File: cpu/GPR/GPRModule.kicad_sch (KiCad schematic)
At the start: 51 parts, among them J1 Interconnect, U1 74HCT574, U10 74HCT245, U11 74HCT125, U2 74HCT574, U3 74HCT245, U4 74HCT245, U5 74HCT245, U6 74HCT245, U7 74HCT245, U8 74HCT245, U9 74HCT245

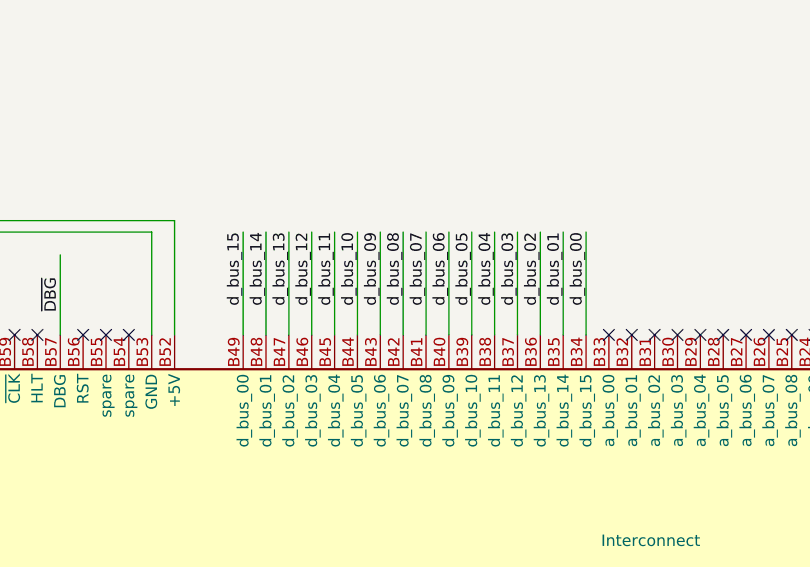
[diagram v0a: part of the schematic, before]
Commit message: GPR v1.4, removed old src, deleted a BOM
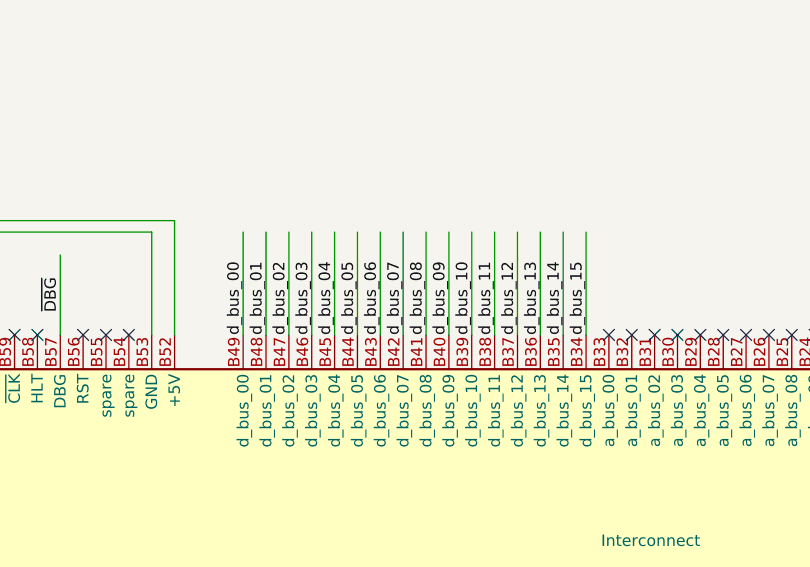
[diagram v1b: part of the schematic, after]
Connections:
- net d_bus_00: now also J1.B49 (d_bus_00); no longer J1.B34 (d_bus_15)
- net d_bus_01: now also J1.B48 (d_bus_01); no longer J1.B35 (d_bus_14)
- net d_bus_02: now also J1.B47 (d_bus_02); no longer J1.B36 (d_bus_13)
- net d_bus_03: now also J1.B46 (d_bus_03); no longer J1.B37 (d_bus_12)
- net d_bus_04: now also J1.B45 (d_bus_04); no longer J1.B38 (d_bus_11)
- net d_bus_05: now also J1.B44 (d_bus_05); no longer J1.B39 (d_bus_10)
- net d_bus_06: now also J1.B43 (d_bus_06); no longer J1.B40 (d_bus_09)
- net d_bus_07: now also J1.B42 (d_bus_07); no longer J1.B41 (d_bus_08)
- net d_bus_08: now also J1.B41 (d_bus_08); no longer J1.B42 (d_bus_07)
- net d_bus_09: now also J1.B40 (d_bus_09); no longer J1.B43 (d_bus_06)
- net d_bus_10: now also J1.B39 (d_bus_10); no longer J1.B44 (d_bus_05)
- net d_bus_11: now also J1.B38 (d_bus_11); no longer J1.B45 (d_bus_04)
- net d_bus_12: now also J1.B37 (d_bus_12); no longer J1.B46 (d_bus_03)
- net d_bus_13: now also J1.B36 (d_bus_13); no longer J1.B47 (d_bus_02)
- net d_bus_14: now also J1.B35 (d_bus_14); no longer J1.B48 (d_bus_01)
- net d_bus_15: now also J1.B34 (d_bus_15); no longer J1.B49 (d_bus_00)
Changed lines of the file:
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@@
     (title "General Purpose Register")
     (date "2020-12-25")
-    (rev "1.3")
+    (rev "1.4")
     (comment 1 "Does not use CLK signal for operation")
   )
@@
     (stroke (width 0) (type default) (color 0 0 0 0))
   )
-  (wire (pts (xy 128.27 194.31) (xy 128.27 182.88))
+  (wire (pts (xy 100.33 182.88) (xy 100.33 194.31))
     (stroke (width 0) (type default) (color 0 0 0 0))
   )
@@
     (stroke (width 0) (type default) (color 0 0 0 0))
   )
-  (wire (pts (xy 115.57 194.31) (xy 115.57 182.88))
+  (wire (pts (xy 113.03 182.88) (xy 113.03 194.31))
     (stroke (width 0) (type default) (color 0 0 0 0))
   )
@@
     (stroke (width 0) (type default) (color 0 0 0 0))
   )
-  (wire (pts (xy 118.11 194.31) (xy 118.11 182.88))
+  (wire (pts (xy 110.49 182.88) (xy 110.49 194.31))
     (stroke (width 0) (type default) (color 0 0 0 0))
   )
@@
     (stroke (width 0) (type default) (color 0 0 0 0))
   )
-  (wire (pts (xy 123.19 194.31) (xy 123.19 182.88))
+  (wire (pts (xy 105.41 182.88) (xy 105.41 194.31))
     (stroke (width 0) (type default) (color 0 0 0 0))
   )
@@
     (stroke (width 0) (type default) (color 0 0 0 0))
   )
-  (wire (pts (xy 120.65 194.31) (xy 120.65 182.88))
+  (wire (pts (xy 107.95 182.88) (xy 107.95 194.31))
     (stroke (width 0) (type default) (color 0 0 0 0))
   )
@@
     (stroke (width 0) (type default) (color 0 0 0 0))
   )
-  (wire (pts (xy 113.03 194.31) (xy 113.03 182.88))
+  (wire (pts (xy 115.57 182.88) (xy 115.57 194.31))
     (stroke (width 0) (type default) (color 0 0 0 0))
   )
@@
     (stroke (width 0) (type default) (color 0 0 0 0))
   )
-  (wire (pts (xy 107.95 194.31) (xy 107.95 182.88))
+  (wire (pts (xy 120.65 182.88) (xy 120.65 194.31))
     (stroke (width 0) (type default) (color 0 0 0 0))
   )
@@
     (stroke (width 0) (type default) (color 0 0 0 0))
   )
-  (wire (pts (xy 102.87 194.31) (xy 102.87 182.88))
+  (wire (pts (xy 125.73 182.88) (xy 125.73 194.31))
     (stroke (width 0) (type default) (color 0 0 0 0))
   )
@@
     (stroke (width 0) (type default) (color 0 0 0 0))
   )
-  (wire (pts (xy 130.81 194.31) (xy 130.81 182.88))
+  (wire (pts (xy 97.79 182.88) (xy 97.79 194.31))
     (stroke (width 0) (type default) (color 0 0 0 0))
   )
@@
     (stroke (width 0) (type default) (color 0 0 0 0))
   )
-  (wire (pts (xy 100.33 194.31) (xy 100.33 182.88))
+  (wire (pts (xy 128.27 182.88) (xy 128.27 194.31))
     (stroke (width 0) (type default) (color 0 0 0 0))
   )
@@
     (stroke (width 0) (type default) (color 0 0 0 0))
   )
-  (wire (pts (xy 110.49 194.31) (xy 110.49 182.88))
+  (wire (pts (xy 118.11 182.88) (xy 118.11 194.31))
     (stroke (width 0) (type default) (color 0 0 0 0))
   )
@@
     (stroke (width 0) (type default) (color 0 0 0 0))
   )
-  (wire (pts (xy 125.73 194.31) (xy 125.73 182.88))
+  (wire (pts (xy 102.87 182.88) (xy 102.87 194.31))
     (stroke (width 0) (type default) (color 0 0 0 0))
   )
@@
     (stroke (width 0) (type default) (color 0 0 0 0))
   )
-  (wire (pts (xy 95.25 194.31) (xy 95.25 182.88))
+  (wire (pts (xy 133.35 182.88) (xy 133.35 194.31))
     (stroke (width 0) (type default) (color 0 0 0 0))
   )
@@
     (stroke (width 0) (type default) (color 0 0 0 0))
   )
-  (wire (pts (xy 105.41 194.31) (xy 105.41 182.88))
+  (wire (pts (xy 123.19 182.88) (xy 123.19 194.31))
     (stroke (width 0) (type default) (color 0 0 0 0))
   )
@@
     (stroke (width 0) (type default) (color 0 0 0 0))
   )
-  (wire (pts (xy 97.79 194.31) (xy 97.79 182.88))
+  (wire (pts (xy 130.81 182.88) (xy 130.81 194.31))
     (stroke (width 0) (type default) (color 0 0 0 0))
   )
@@
     (stroke (width 0) (type default) (color 0 0 0 0))
   )
-  (wire (pts (xy 133.35 194.31) (xy 133.35 182.88))
+  (wire (pts (xy 95.25 182.88) (xy 95.25 194.31))
     (stroke (width 0) (type default) (color 0 0 0 0))
   )
@@
     (effects (font (size 1.27 1.27)) (justify right bottom))
   )
-  (label "d_bus_01" (at 130.81 182.88 270)
-    (effects (font (size 1.27 1.27)) (justify right bottom))
-  )
-  (label "d_bus_11" (at 105.41 182.88 270)
-    (effects (font (size 1.27 1.27)) (justify right bottom))
+  (label "d_bus_01" (at 97.79 194.31 90)
+    (effects (font (size 1.27 1.27)) (justify left bottom))
+  )
+  (label "d_bus_11" (at 123.19 194.31 90)
+    (effects (font (size 1.27 1.27)) (justify left bottom))
   )
   (label "y_bus_12" (at 342.9 30.48 270)
@@
     (effects (font (size 1.27 1.27)) (justify left bottom))
   )
-  (label "d_bus_04" (at 123.19 182.88 270)
-    (effects (font (size 1.27 1.27)) (justify right bottom))
+  (label "d_bus_04" (at 105.41 194.31 90)
+    (effects (font (size 1.27 1.27)) (justify left bottom))
   )
   (label "d_bus_02" (at 49.53 137.16 90)
@@
     (effects (font (size 1.27 1.27)) (justify left bottom))
   )
-  (label "d_bus_00" (at 133.35 182.88 270)
-    (effects (font (size 1.27 1.27)) (justify right bottom))
+  (label "d_bus_00" (at 95.25 194.31 90)
+    (effects (font (size 1.27 1.27)) (justify left bottom))
   )
   (label "x_bus_09" (at 118.11 251.46 90)
@@
     (effects (font (size 1.27 1.27)) (justify right bottom))
   )
-  (label "d_bus_15" (at 95.25 182.88 270)
-    (effects (font (size 1.27 1.27)) (justify right bottom))
+  (label "d_bus_15" (at 133.35 194.31 90)
+    (effects (font (size 1.27 1.27)) (justify left bottom))
   )
   (label "x_bus_04" (at 105.41 251.46 90)
@@
     (effects (font (size 1.27 1.27)) (justify right bottom))
   )
-  (label "d_bus_12" (at 102.87 182.88 270)
-    (effects (font (size 1.27 1.27)) (justify right bottom))
+  (label "d_bus_12" (at 125.73 194.31 90)
+    (effects (font (size 1.27 1.27)) (justify left bottom))
   )
   (label "d_bus_15" (at 58.42 30.48 270)
@@
     (effects (font (size 1.27 1.27)) (justify right bottom))
   )
-  (label "d_bus_08" (at 113.03 182.88 270)
-    (effects (font (size 1.27 1.27)) (justify right bottom))
+  (label "d_bus_08" (at 115.57 194.31 90)
+    (effects (font (size 1.27 1.27)) (justify left bottom))
   )
   (label "y_bus_04" (at 146.05 251.46 90)
@@
     (effects (font (size 1.27 1.27)) (justify left bottom))
   )
-  (label "d_bus_09" (at 110.49 182.88 270)
-    (effects (font (size 1.27 1.27)) (justify right bottom))
+  (label "d_bus_09" (at 118.11 194.31 90)
+    (effects (font (size 1.27 1.27)) (justify left bottom))
   )
   (label "reg_11" (at 328.93 90.17 270)
@@
     (effects (font (size 1.27 1.27)) (justify left bottom))
   )
-  (label "d_bus_10" (at 107.95 182.88 270)
-    (effects (font (size 1.27 1.27)) (justify right bottom))
+  (label "d_bus_10" (at 120.65 194.31 90)
+    (effects (font (size 1.27 1.27)) (justify left bottom))
   )
   (label "reg_02" (at 114.3 78.74 90)
@@
     (effects (font (size 1.27 1.27)) (justify left bottom))
   )
-  (label "d_bus_05" (at 120.65 182.88 270)
-    (effects (font (size 1.27 1.27)) (justify right bottom))
+  (label "d_bus_05" (at 107.95 194.31 90)
+    (effects (font (size 1.27 1.27)) (justify left bottom))
   )
   (label "y_bus_10" (at 161.29 251.46 90)
@@
     (effects (font (size 1.27 1.27)) (justify left bottom))
   )
-  (label "d_bus_03" (at 125.73 182.88 270)
-    (effects (font (size 1.27 1.27)) (justify right bottom))
+  (label "d_bus_03" (at 102.87 194.31 90)
+    (effects (font (size 1.27 1.27)) (justify left bottom))
   )
   (label "reg_08" (at 353.06 78.74 90)
@@
     (effects (font (size 1.27 1.27)) (justify left bottom))
   )
-  (label "d_bus_07" (at 115.57 182.88 270)
-    (effects (font (size 1.27 1.27)) (justify right bottom))
+  (label "d_bus_07" (at 113.03 194.31 90)
+    (effects (font (size 1.27 1.27)) (justify left bottom))
   )
   (label "reg_06" (at 381 78.74 90)
@@
     (effects (font (size 1.27 1.27)) (justify left bottom))
   )
-  (label "d_bus_14" (at 97.79 182.88 270)
-    (effects (font (size 1.27 1.27)) (justify right bottom))
+  (label "d_bus_14" (at 130.81 194.31 90)
+    (effects (font (size 1.27 1.27)) (justify left bottom))
   )
   (label "reg_14" (at 60.96 78.74 90)
@@
     (effects (font (size 1.27 1.27)) (justify left bottom))
   )
-  (label "d_bus_06" (at 118.11 182.88 270)
-    (effects (font (size 1.27 1.27)) (justify right bottom))
+  (label "d_bus_06" (at 110.49 194.31 90)
+    (effects (font (size 1.27 1.27)) (justify left bottom))
   )
   (label "reg_09" (at 73.66 78.74 90)
@@
     (effects (font (size 1.27 1.27)) (justify left bottom))
   )
-  (label "d_bus_02" (at 128.27 182.88 270)
-    (effects (font (size 1.27 1.27)) (justify right bottom))
+  (label "d_bus_02" (at 100.33 194.31 90)
+    (effects (font (size 1.27 1.27)) (justify left bottom))
   )
   (label "x_bus_13" (at 200.66 30.48 270)
@@
     (effects (font (size 1.27 1.27)) (justify left bottom))
   )
-  (label "d_bus_13" (at 100.33 182.88 270)
-    (effects (font (size 1.27 1.27)) (justify right bottom))
+  (label "d_bus_13" (at 128.27 194.31 90)
+    (effects (font (size 1.27 1.27)) (justify left bottom))
   )
   (label "x_bus_08" (at 115.57 251.46 90)
